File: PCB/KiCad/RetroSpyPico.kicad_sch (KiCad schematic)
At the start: 14 parts, among them CN1 Conn_02x05_Row_Letter_First, CN2 Conn_02x05_Row_Letter_First, SW1 SW_SPDT, SW2 SW_Push, U1 Raspberry Pi Pico

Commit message: add comment
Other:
- note added: "Disable the built-in pull-up and pull-down resistors and input the SNES signals divided by 10kΩ and 20kΩ (10+10kΩ) external resistors. If the resistance value used for voltage division is too low, SNES and RetroSpy will recognize that all buttons are being pressed when no controller is connected."
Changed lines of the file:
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@@
   (title_block
     (title "RetroSpy for Raspberry Pi Pico")
-    (date "2023-01-11")
+    (date "2023-03-07")
     (rev "1")
     (company "T.T")
@@
     (effects (font (size 1.27 1.27)) (justify right bottom))
   )
+  (text "Disable the built-in pull-up and pull-down resistors\nand input the SNES signals divided by 10kΩ and 20kΩ (10+10kΩ) external resistors.\n\nIf the resistance value used for voltage division is too low,\nSNES and RetroSpy will recognize that all buttons are being pressed when no controller is connected."
+    (at 166.37 139.7 0)
+    (effects (font (size 1.27 1.27)) (justify left bottom))
+  )
   (text "SNES controller" (at 231.14 86.36 0)

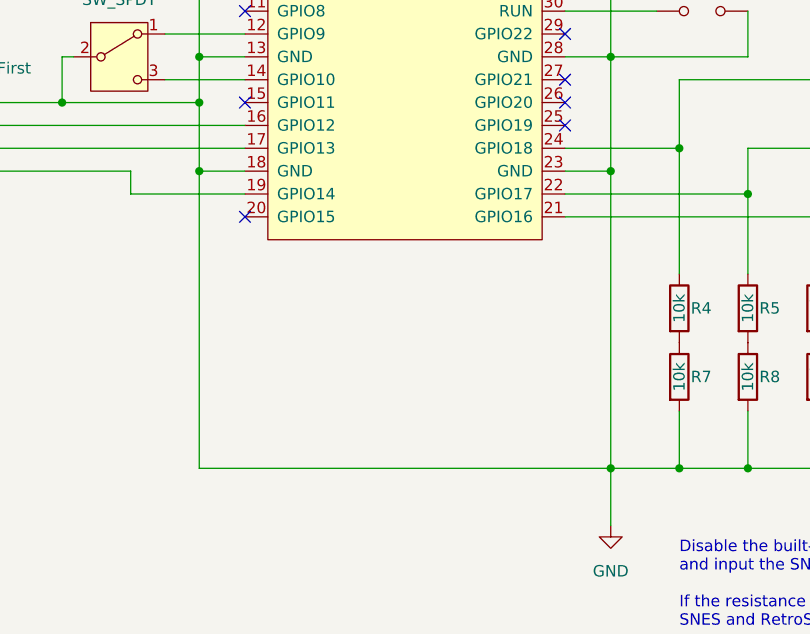
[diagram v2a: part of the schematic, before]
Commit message: Allows Raspberry Pi Pico to be soldered directly to the board without pin headers.
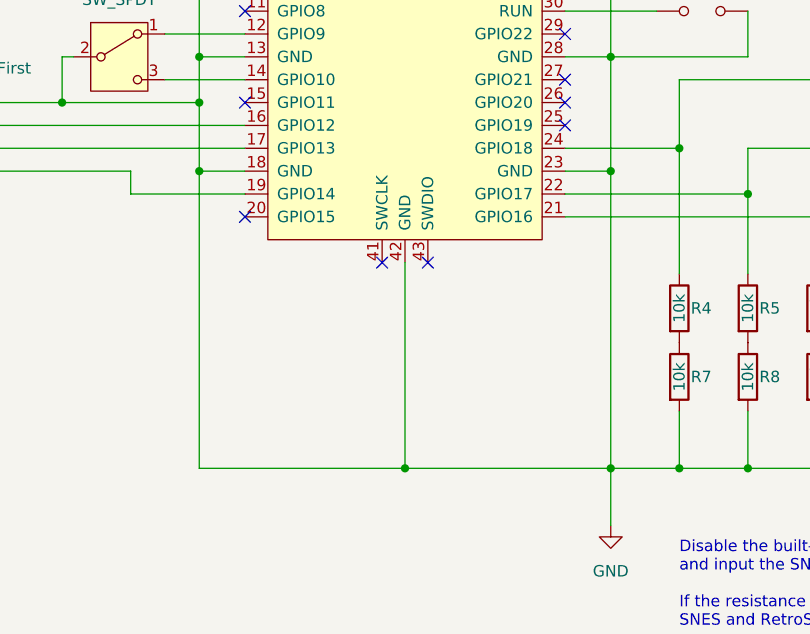
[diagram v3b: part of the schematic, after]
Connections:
- net GND: now also U1.42 (GND)
- no-connect marks 23 -> 25
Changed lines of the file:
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@@
 	(title_block
 		(title "RetroSpy for Raspberry Pi Pico")
-		(date "2023-03-07")
-		(rev "1")
+		(date "2024-03-24")
+		(rev "2")
 		(company "T.T")
 	)
@@
 	)
 	(junction
+		(at 135.89 121.92)
+		(diameter 0)
+		(color 0 0 0 0)
+	)
+	(junction
 		(at 158.75 121.92)
 		(diameter 0)
@@
 	)
 	(no_connect
+		(at 133.35 99.06)
+	)
+	(no_connect
 		(at 118.11 60.96)
 	)
@@
 	)
 	(no_connect
+		(at 138.43 99.06)
+	)
+	(no_connect
 		(at 118.11 81.28)
 	)
@@
 	(wire
 		(pts
-			(xy 113.03 121.92) (xy 158.75 121.92)
+			(xy 113.03 121.92) (xy 135.89 121.92)
 		)
 		(stroke
@@
 	(wire
 		(pts
+			(xy 135.89 99.06) (xy 135.89 121.92)
+		)
+		(stroke
+			(width 0)
+			(type default)
+		)
+	)
+	(wire
+		(pts
 			(xy 173.99 91.44) (xy 173.99 100.33)
 		)
@@
 		(pts
 			(xy 118.11 63.5) (xy 113.03 63.5)
+		)
+		(stroke
+			(width 0)
+			(type default)
+		)
+	)
+	(wire
+		(pts
+			(xy 135.89 121.92) (xy 158.75 121.92)
 		)
 		(stroke
@@
 		(pin "9"
 		)
+		(pin "41"
+		)
+		(pin "42"
+		)
+		(pin "43"
+		)
 		(instances
